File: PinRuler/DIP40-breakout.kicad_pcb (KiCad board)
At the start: 2 copper layers, 52.2 x 27.7 mm, 2 parts, among them J1 Conn_02x20_Counter_Clockwise, J2 Conn_02x20_Counter_Clockwise

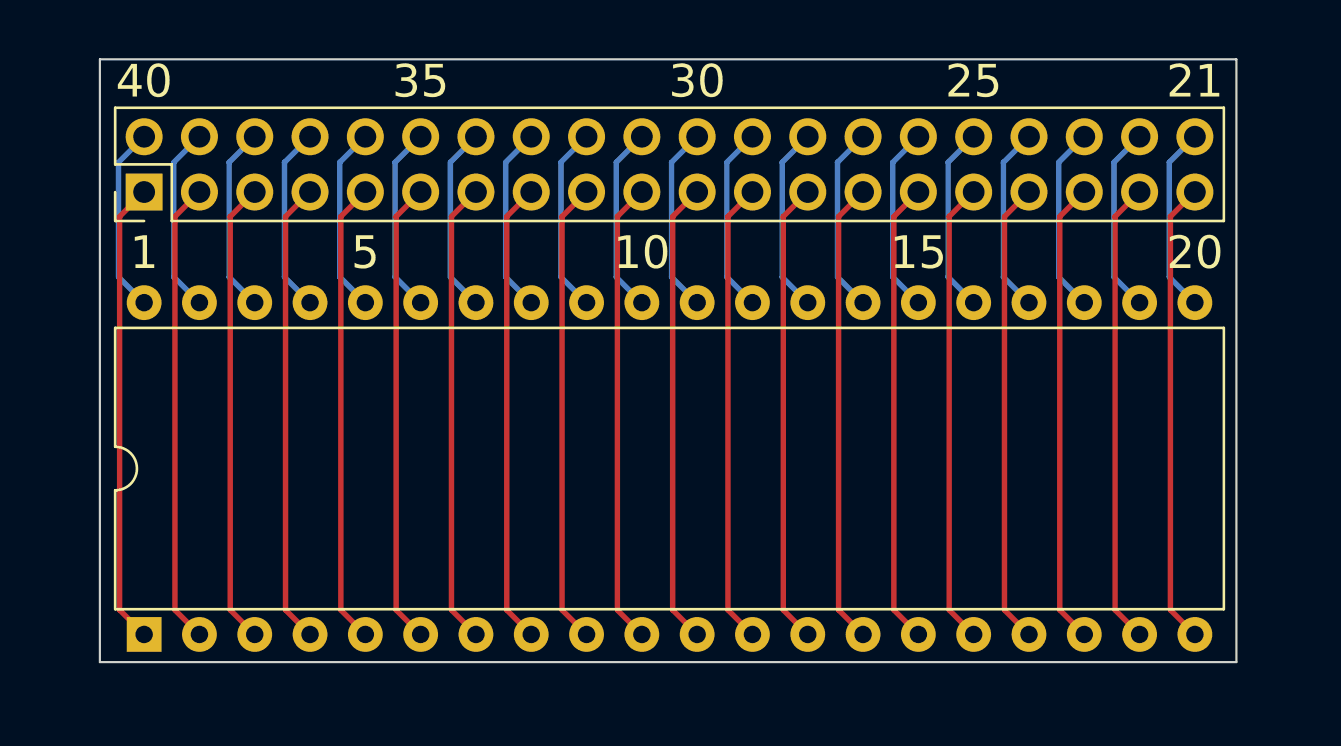
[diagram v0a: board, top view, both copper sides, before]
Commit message: Chip breakout boards use larger holes to allow for precision sockets to go through
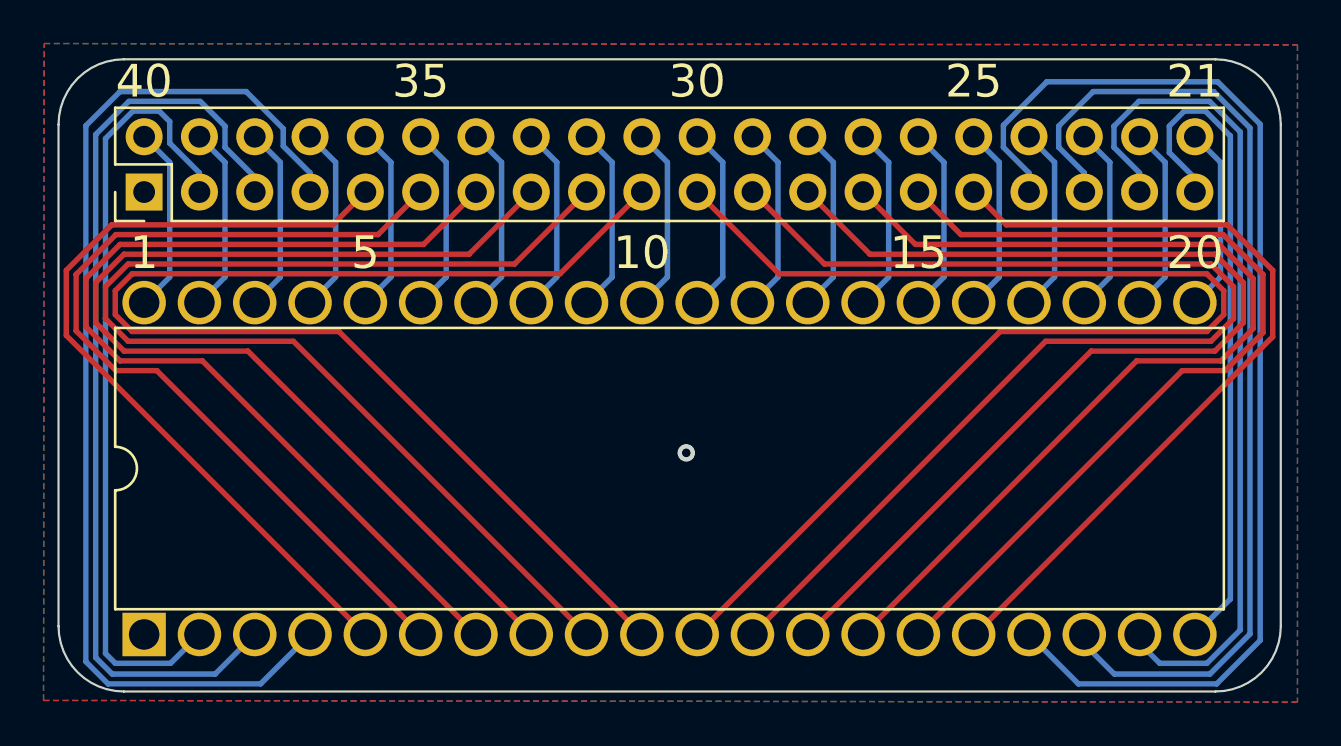
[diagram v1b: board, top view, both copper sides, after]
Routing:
- net Net-(J1-Pin_10): track 21.3 -> 57.4 mm
- net Net-(J1-Pin_11): track 21.3 -> 57.4 mm
- net Net-(J1-Pin_9): track 21.3 -> 53.5 mm
- net Net-(J1-Pin_12): track 21.3 -> 53.5 mm
- net Net-(J1-Pin_17): track 21.3 -> 53.1 mm
- net Net-(J1-Pin_4): track 21.3 -> 50.1 mm
- net Net-(J1-Pin_13): track 21.3 -> 49.5 mm
- net Net-(J1-Pin_8): track 21.3 -> 49.5 mm
- net Net-(J1-Pin_18): track 21.3 -> 45.8 mm
- net Net-(J1-Pin_14): track 21.3 -> 45.6 mm
- net Net-(J1-Pin_7): track 21.3 -> 45.5 mm
- net Net-(J1-Pin_3): track 21.3 -> 43.0 mm
- net Net-(J1-Pin_1): track 21.3 -> 0.00 mm, vias 0 -> 1
- net Net-(J1-Pin_15): track 21.3 -> 41.6 mm
- net Net-(J1-Pin_6): track 21.3 -> 41.6 mm
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- added copper zone on B.Cu, net Net-(J1-Pin_1)
- added copper zone on F.Cu, net Net-(J1-Pin_1)
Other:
- board size 52.2 x 27.7 mm -> 56.1 x 29 mm
